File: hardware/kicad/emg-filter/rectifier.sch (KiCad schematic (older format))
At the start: 8 parts, among them U1 LM4565

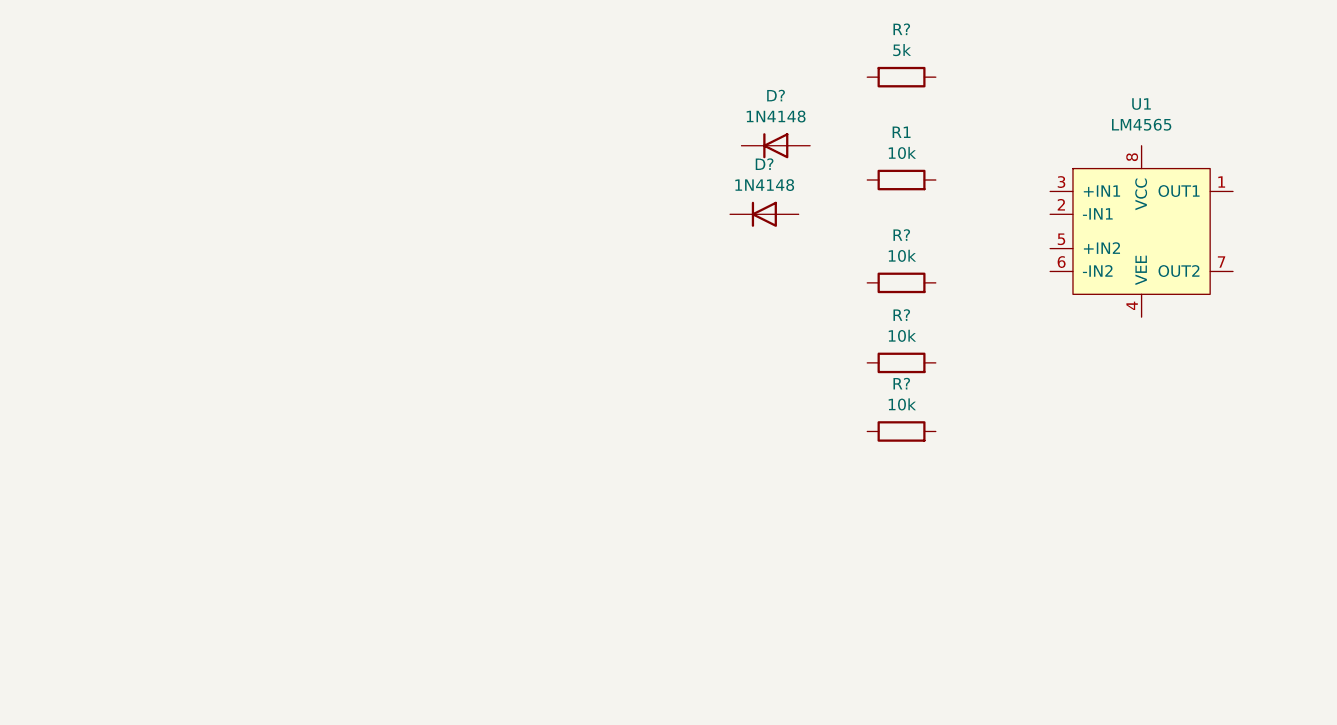
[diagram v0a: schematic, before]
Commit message: Added rectifier diagram
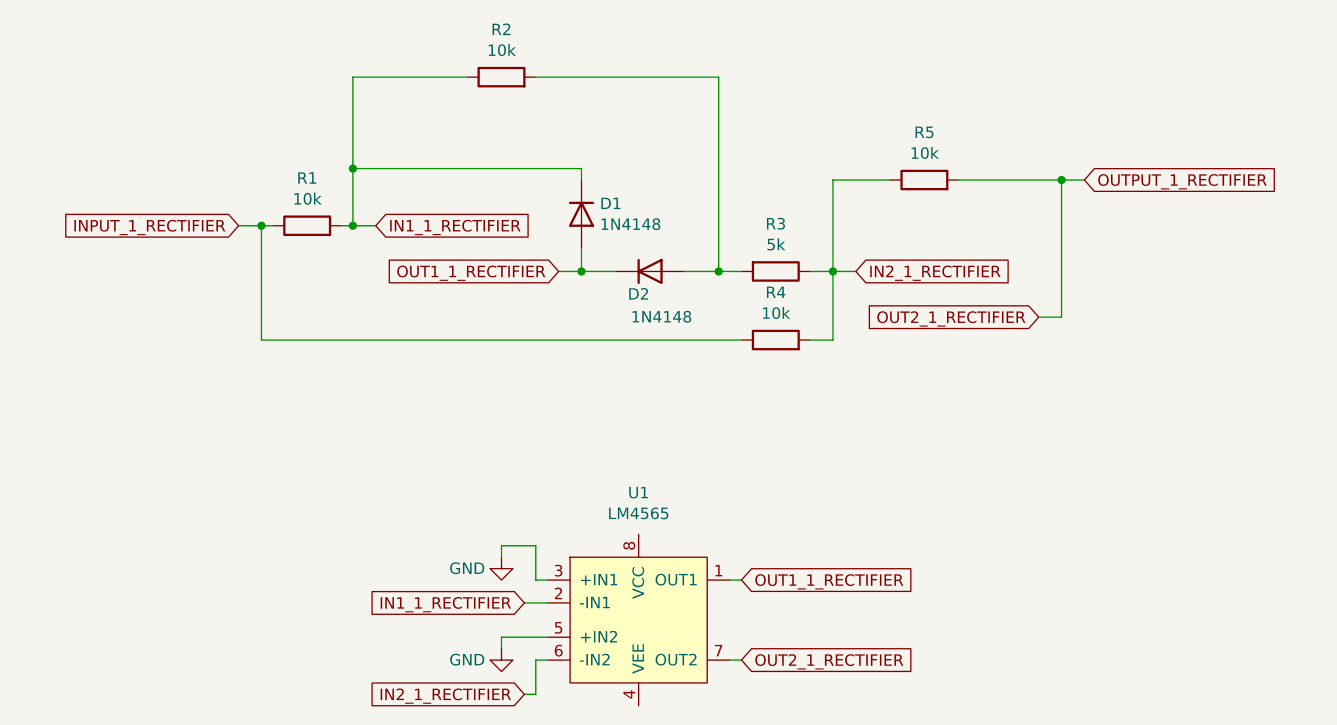
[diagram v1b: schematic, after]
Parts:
- gave numbers to parts that had none: 6
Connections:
- net OUT1_1_RECTIFIER: now reaches U1.1 (OUT1)
- net OUT1_1_RECTIFIER: now also D1.2 (A), D2.1 (K)
- net IN1_1_RECTIFIER: now reaches U1.2 (-IN1)
- net IN1_1_RECTIFIER: now also D1.1 (K), R1.2, R2.1
- net GND: now reaches U1.3 (+IN1)
- net GND: now also U1.5 (+IN2)
- net IN2_1_RECTIFIER: now reaches U1.6 (-IN2)
- net IN2_1_RECTIFIER: now also R3.1, R4.2, R5.1
- net OUT2_1_RECTIFIER: now reaches U1.7 (OUT2)
- net OUT2_1_RECTIFIER: now also R5.2
- net INPUT_1_RECTIFIER: now reaches R1.1
- net INPUT_1_RECTIFIER: now also R4.1
- net at R2.2: now also D2.2 (A), R3.2
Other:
- moved on the sheet: D1, D2, R1, R2, R3, R4, R5, U1
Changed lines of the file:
@@
 L emg-filter:LM4565 U1
 U 1 1 61C39F82
-P 7050 2900
-F 0 "U1" H 7050 3431 50  0000 C CNN
-F 1 "LM4565" H 7050 3340 50  0000 C CNN
-F 2 "" H 8050 2900 50  0001 C CNN
-F 3 "" H 8050 2900 50  0001 C CNN
-	1    7050 2900
+P 4850 4600
+F 0 "U1" H 4850 5131 50  0000 C CNN
+F 1 "LM4565" H 4850 5040 50  0000 C CNN
+F 2 "" H 5850 4600 50  0001 C CNN
+F 3 "" H 5850 4600 50  0001 C CNN
+	1    4850 4600
 	1    0    0    -1
 $EndComp
@@
 L Device:R R1
 U 1 1 61C3AD78
-P 6000 2700
-F 0 "R1" V 6207 2700 50  0000 C CNN
-F 1 "10k" V 6116 2700 50  0000 C CNN
-F 2 "" V 5930 2700 50  0001 C CNN
-F 3 "~" H 6000 2700 50  0001 C CNN
-	1    6000 2700
-	0    -1   -1   0
-$EndComp
-$Comp
-L Device:R R?
+P 3400 2900
+F 0 "R1" V 3607 2900 50  0000 C CNN
+F 1 "10k" V 3516 2900 50  0000 C CNN
+F 2 "" V 3330 2900 50  0001 C CNN
+F 3 "~" H 3400 2900 50  0001 C CNN
+	1    3400 2900
+	0    -1   -1   0
+$EndComp
+$Comp
+L Device:R R2
 U 1 1 61C4805B
-P 6000 3150
-F 0 "R?" V 6207 3150 50  0000 C CNN
-F 1 "10k" V 6116 3150 50  0000 C CNN
-F 2 "" V 5930 3150 50  0001 C CNN
-F 3 "~" H 6000 3150 50  0001 C CNN
-	1    6000 3150
-	0    -1   -1   0
-$EndComp
-$Comp
-L Device:R R?
+P 4250 2250
+F 0 "R2" V 4457 2250 50  0000 C CNN
+F 1 "10k" V 4366 2250 50  0000 C CNN
+F 2 "" V 4180 2250 50  0001 C CNN
+F 3 "~" H 4250 2250 50  0001 C CNN
+	1    4250 2250
+	0    -1   -1   0
+$EndComp
+$Comp
+L Device:R R3
 U 1 1 61C4A9A1
-P 6000 2250
-F 0 "R?" V 5793 2250 50  0000 C CNN
-F 1 "5k" V 5884 2250 50  0000 C CNN
-F 2 "" V 5930 2250 50  0001 C CNN
-F 3 "~" H 6000 2250 50  0001 C CNN
-	1    6000 2250
+P 5450 3100
+F 0 "R3" V 5243 3100 50  0000 C CNN
+F 1 "5k" V 5334 3100 50  0000 C CNN
+F 2 "" V 5380 3100 50  0001 C CNN
+F 3 "~" H 5450 3100 50  0001 C CNN
+	1    5450 3100
 	0    1    1    0
 $EndComp
 $Comp
-L Device:R R?
+L Device:R R5
 U 1 1 61C4B3BB
-P 6000 3500
-F 0 "R?" V 6207 3500 50  0000 C CNN
-F 1 "10k" V 6116 3500 50  0000 C CNN
-F 2 "" V 5930 3500 50  0001 C CNN
-F 3 "~" H 6000 3500 50  0001 C CNN
-	1    6000 3500
-	0    -1   -1   0
-$EndComp
-$Comp
-L Device:R R?
+P 6100 2700
+F 0 "R5" V 6307 2700 50  0000 C CNN
+F 1 "10k" V 6216 2700 50  0000 C CNN
+F 2 "" V 6030 2700 50  0001 C CNN
+F 3 "~" H 6100 2700 50  0001 C CNN
+	1    6100 2700
+	0    -1   -1   0
+$EndComp
+$Comp
+L Device:R R4
 U 1 1 61C4B97C
-P 6000 3800
-F 0 "R?" V 6207 3800 50  0000 C CNN
-F 1 "10k" V 6116 3800 50  0000 C CNN
-F 2 "" V 5930 3800 50  0001 C CNN
-F 3 "~" H 6000 3800 50  0001 C CNN
-	1    6000 3800
-	0    -1   -1   0
-$EndComp
-$Comp
-L Device:D D?
+P 5450 3400
+F 0 "R4" V 5657 3400 50  0000 C CNN
+F 1 "10k" V 5566 3400 50  0000 C CNN
+F 2 "" V 5380 3400 50  0001 C CNN
+F 3 "~" H 5450 3400 50  0001 C CNN
+	1    5450 3400
+	0    -1   -1   0
+$EndComp
+$Comp
+L Device:D D2
 U 1 1 61C4C7DA
-P 5450 2550
-F 0 "D?" H 5450 2767 50  0000 C CNN
-F 1 "1N4148" H 5450 2676 50  0000 C CNN
-F 2 "" H 5450 2550 50  0001 C CNN
-F 3 "~" H 5450 2550 50  0001 C CNN
-	1    5450 2550
-	1    0    0    -1
-$EndComp
-$Comp
-L Device:D D?
+P 4900 3100
+F 0 "D2" H 4850 3000 50  0000 C CNN
+F 1 "1N4148" H 4950 2900 50  0000 C CNN
+F 2 "" H 4900 3100 50  0001 C CNN
+F 3 "~" H 4900 3100 50  0001 C CNN
+	1    4900 3100
+	1    0    0    -1
+$EndComp
+$Comp
+L Device:D D1
 U 1 1 61C4C9DB
-P 5400 2850
-F 0 "D?" H 5400 3067 50  0000 C CNN
-F 1 "1N4148" H 5400 2976 50  0000 C CNN
-F 2 "" H 5400 2850 50  0001 C CNN
-F 3 "~" H 5400 2850 50  0001 C CNN
-	1    5400 2850
-	1    0    0    -1
-$EndComp
+P 4600 2850
+F 0 "D1" V 4554 2930 50  0000 L CNN
+F 1 "1N4148" V 4645 2930 50  0000 L CNN
+F 2 "" H 4600 2850 50  0001 C CNN
+F 3 "~" H 4600 2850 50  0001 C CNN
+	1    4600 2850
+	0    1    1    0
+$EndComp
+Wire Wire Line
+	3600 2250 4100 2250
+Wire Wire Line
+	4600 2700 4600 2650
+Wire Wire Line
+	4600 2650 3600 2650
+Wire Wire Line
+	3600 2650 3600 2250
+Wire Wire Line
+	3600 2650 3600 2900
+Wire Wire Line
+	3600 2900 3550 2900
+Connection ~ 3600 2650
+Text GLabel 5300 4450 2    50   Input ~ 0
+OUT1_1_RECTIFIER
+Text GLabel 4500 3100 0    50   Input ~ 0
+OUT1_1_RECTIFIER
+Wire Wire Line
+	4600 3000 4600 3100
+Wire Wire Line
+	5200 3100 5200 2250
+Wire Wire Line
+	5200 2250 4400 2250
+Wire Wire Line
+	5200 3100 5300 3100
+Wire Wire Line
+	4600 3100 4750 3100
+Wire Wire Line
+	5050 3100 5200 3100
+Connection ~ 5200 3100
+Text GLabel 3700 2900 2    50   Input ~ 0
+IN1_1_RECTIFIER
+Wire Wire Line
+	4500 3100 4600 3100
+Connection ~ 4600 3100
+Wire Wire Line
+	3600 2900 3700 2900
+Connection ~ 3600 2900
+Text GLabel 4350 4550 0    50   Input ~ 0
+IN1_1_RECTIFIER
+Wire Wire Line
+	5250 4450 5300 4450
+$Comp
+L power:GND #PWR01
+U 1 1 61C650AA
+P 4250 4350
+F 0 "#PWR01" H 4250 4100 50  0001 C CNN
+F 1 "GND" H 4100 4300 50  0000 C CNN
+F 2 "" H 4250 4350 50  0001 C CNN
+F 3 "" H 4250 4350 50  0001 C CNN
+	1    4250 4350
+	1    0    0    -1
+$EndComp
+Wire Wire Line
+	3250 2900 3200 2900
+Wire Wire Line
+	3200 3400 5300 3400
+Wire Wire Line
+	3200 2900 3200 3400
+Wire Wire Line
+	5600 3400 5700 3400
+Wire Wire Line
+	5700 3400 5700 3100
+Wire Wire Line
+	5700 3100 5600 3100
+Wire Wire Line
+	5700 3100 5700 2700
+Wire Wire Line
+	5700 2700 5950 2700
+Connection ~ 5700 3100
+Text GLabel 5800 3100 2    50   Input ~ 0
+IN2_1_RECTIFIER
+Wire Wire Line
+	5700 3100 5800 3100
+Text GLabel 4350 4950 0    50   Input ~ 0
+IN2_1_RECTIFIER
+$Comp
+L power:GND #PWR02
+U 1 1 61C6C0BF
+P 4250 4750
+F 0 "#PWR02" H 4250 4500 50  0001 C CNN
+F 1 "GND" H 4100 4700 50  0000 C CNN
+F 2 "" H 4250 4750 50  0001 C CNN
+F 3 "" H 4250 4750 50  0001 C CNN
+	1    4250 4750
+	1    0    0    -1
+$EndComp
+Wire Wire Line
+	4450 4700 4250 4700
+Wire Wire Line
+	4450 4550 4350 4550
+Text GLabel 5300 4800 2    50   Input ~ 0
+OUT2_1_RECTIFIER
+Wire Wire Line
+	5250 4800 5300 4800
+Text GLabel 6600 3300 0    50   Input ~ 0
+OUT2_1_RECTIFIER
+Wire Wire Line
+	6600 3300 6700 3300
+Wire Wire Line
+	6700 3300 6700 2700
+Wire Wire Line
+	6700 2700 6250 2700
+Wire Wire Line
+	4450 4800 4400 4800
+Wire Wire Line
+	4400 4800 4400 4950
+Wire Wire Line
+	4400 4950 4350 4950
+Wire Wire Line
+	4450 4450 4400 4450
+Wire Wire Line
+	4400 4450 4400 4300
+Wire Wire Line
+	4400 4300 4250 4300
+Text GLabel 3100 2900 0    50   Input ~ 0
+INPUT_1_RECTIFIER
+Wire Wire Line
+	3200 2900 3100 2900
+Connection ~ 3200 2900
+Text GLabel 6800 2700 2    50   Input ~ 0
+OUTPUT_1_RECTIFIER
+Wire Wire Line
+	6800 2700 6700 2700
+Connection ~ 6700 2700
+Wire Wire Line
+	4250 4700 4250 4750
+Wire Wire Line
+	4250 4300 4250 4350
 $EndSCHEMATC

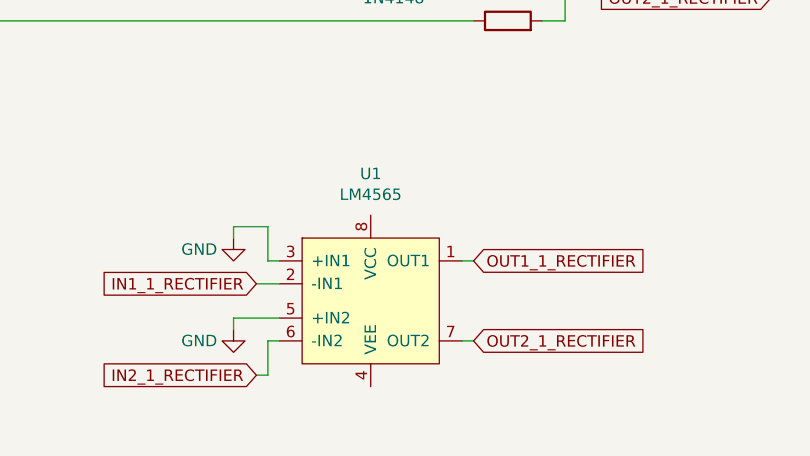
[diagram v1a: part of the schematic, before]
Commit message: Rectifier implemented
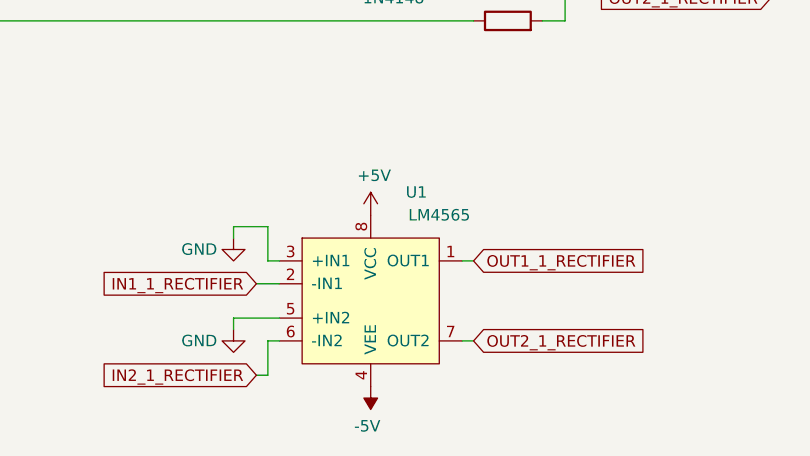
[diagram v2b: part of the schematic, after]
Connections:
- net -5V: now reaches U1.4 (VEE)
- net +5V: now reaches U1.8 (VCC)
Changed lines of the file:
@@
 U 1 1 61C39F82
 P 4850 4600
-F 0 "U1" H 4850 5131 50  0000 C CNN
-F 1 "LM4565" H 4850 5040 50  0000 C CNN
+F 0 "U1" H 5050 5050 50  0000 C CNN
+F 1 "LM4565" H 5150 4950 50  0000 C CNN
 F 2 "" H 5850 4600 50  0001 C CNN
 F 3 "" H 5850 4600 50  0001 C CNN
@@
 Wire Wire Line
 	4250 4300 4250 4350
+$Comp
+L power:+5V #PWR?
+U 1 1 61C415B3
+P 4850 4250
+F 0 "#PWR?" H 4850 4100 50  0001 C CNN
+F 1 "+5V" H 4865 4423 50  0000 C CNN
+F 2 "" H 4850 4250 50  0001 C CNN
+F 3 "" H 4850 4250 50  0001 C CNN
+	1    4850 4250
+	1    0    0    -1
+$EndComp
+$Comp
+L power:-5V #PWR?
+U 1 1 61C41B44
+P 4850 5000
+F 0 "#PWR?" H 4850 5100 50  0001 C CNN
+F 1 "-5V" H 4865 5173 50  0000 C CNN
+F 2 "" H 4850 5000 50  0001 C CNN
+F 3 "" H 4850 5000 50  0001 C CNN
+	1    4850 5000
+	-1   0    0    1
+$EndComp
 $EndSCHEMATC

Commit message: 16 rectifiers.
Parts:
- added D10, D11, D12, D13, D14, D15, D16, D17, D18, D19, D20, D21, D22, D23, D24, D25, D26, D27, D28, D29, D3, D30, D31, D32, D4, D5, D6, D7, D8, D9: 1N4148, symbol Device:D
- added R10, R11, R12, R13, R14, R15, R16, R17, R18, R19, R21, R23, R25, R27, R29, R31, R33, R34, R35, R36, R37, R38, R39, R40, R41, R42, R43, R44, R45, R46, R47, R48, R49, R50, R51, R52, R53, R54, R55, R56, R58, R6, R60, R62, R64, R66, R68, R7, R70, R72, R73, R74, R75, R76, R77, R78, R79, R8, R80, R9: 10k, symbol Device:R
- added R20, R22, R24, R26, R28, R30, R32, R57, R59, R61, R63, R65, R67, R69, R71: 5k, symbol Device:R
- added U10, U11, U12, U13, U14, U15, U16, U2, U3, U4, U5, U6, U7, U8, U9: LM4565, symbol emg-filter:LM4565
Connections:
- net +5V: now also U10.8 (VCC), U11.8 (VCC), U12.8 (VCC), U13.8 (VCC), U14.8 (VCC), U15.8 (VCC), U16.8 (VCC), U2.8 (VCC), U3.8 (VCC), U4.8 (VCC), U5.8 (VCC), U6.8 (VCC), U7.8 (VCC), U8.8 (VCC), U9.8 (VCC)
- net -5V: now also U10.4 (VEE), U11.4 (VEE), U12.4 (VEE), U13.4 (VEE), U14.4 (VEE), U15.4 (VEE), U16.4 (VEE), U2.4 (VEE), U3.4 (VEE), U4.4 (VEE), U5.4 (VEE), U6.4 (VEE), U7.4 (VEE), U8.4 (VEE), U9.4 (VEE)
- net GND: now also U10.3 (+IN1), U10.5 (+IN2), U11.3 (+IN1), U11.5 (+IN2), U12.3 (+IN1), U12.5 (+IN2), U13.3 (+IN1), U13.5 (+IN2), U14.3 (+IN1), U14.5 (+IN2), U15.3 (+IN1), U15.5 (+IN2), U16.3 (+IN1), U16.5 (+IN2), U2.3 (+IN1), U2.5 (+IN2), U3.3 (+IN1), U3.5 (+IN2), U4.3 (+IN1), U4.5 (+IN2), U5.3 (+IN1), U5.5 (+IN2), U6.3 (+IN1), U6.5 (+IN2), U7.3 (+IN1), U7.5 (+IN2), U8.3 (+IN1), U8.5 (+IN2), U9.3 (+IN1), U9.5 (+IN2)
- new net: D10.2 (A), R13.2, R20.2
- new net: D11.2 (A), R14.2, R22.2
- new net: D12.2 (A), R15.2, R24.2
- new net: D13.2 (A), R16.2, R26.2
- new net: D14.2 (A), R17.2, R28.2
- new net: D15.2 (A), R18.2, R30.2
- new net: D16.2 (A), R19.2, R32.2
- new net: D29.2 (A), R53.2, R65.2
- new net: D26.2 (A), R50.2, R59.2
- new net: D27.2 (A), R51.2, R61.2
- new net: D28.2 (A), R52.2, R63.2
- new net: D25.2 (A), R49.2, R57.2
- new net: D31.2 (A), R55.2, R69.2
- new net: D32.2 (A), R56.2, R71.2
- new net: D30.2 (A), R54.2, R67.2
- new net IN1_10_RECTIFIER: D18.1 (K), R42.2, R50.1, U10.2 (-IN1)
- new net IN1_11_RECTIFIER: D19.1 (K), R43.2, R51.1, U11.2 (-IN1)
- new net IN1_12_RECTIFIER: D20.1 (K), R44.2, R52.1, U12.2 (-IN1)
- new net IN1_13_RECTIFIER: D17.1 (K), R41.2, R49.1, U9.2 (-IN1)
- new net IN1_14_RECTIFIER: D23.1 (K), R47.2, R55.1, U15.2 (-IN1)
- new net IN1_15_RECTIFIER: D24.1 (K), R48.2, R56.1, U16.2 (-IN1)
- new net IN1_16_RECTIFIER: D22.1 (K), R46.2, R54.1, U14.2 (-IN1)
- new net IN1_2_RECTIFIER: D3.1 (K), R13.1, R6.2, U2.2 (-IN1)
- new net IN1_3_RECTIFIER: D4.1 (K), R14.1, R7.2, U3.2 (-IN1)
- new net IN1_4_RECTIFIER: D5.1 (K), R15.1, R8.2, U4.2 (-IN1)
- new net IN1_5_RECTIFIER: D6.1 (K), R16.1, R9.2, U5.2 (-IN1)
- new net IN1_6_RECTIFIER: D7.1 (K), R10.2, R17.1, U6.2 (-IN1)
- new net IN1_7_RECTIFIER: D8.1 (K), R11.2, R18.1, U7.2 (-IN1)
- new net IN1_8_RECTIFIER: D9.1 (K), R12.2, R19.1, U8.2 (-IN1)
- new net IN1_9_RECTIFIER: D21.1 (K), R45.2, R53.1, U13.2 (-IN1)
- new net IN2_10_RECTIFIER: R59.1, R60.2, R74.1, U10.6 (-IN2)
- new net IN2_11_RECTIFIER: R61.1, R62.2, R75.1, U11.6 (-IN2)
- new net IN2_12_RECTIFIER: R63.1, R64.2, R76.1, U12.6 (-IN2)
- new net IN2_13_RECTIFIER: R57.1, R58.2, R73.1, U9.6 (-IN2)
- new net IN2_14_RECTIFIER: R69.1, R70.2, R79.1, U15.6 (-IN2)
- new net IN2_15_RECTIFIER: R71.1, R72.2, R80.1, U16.6 (-IN2)
- new net IN2_16_RECTIFIER: R67.1, R68.2, R78.1, U14.6 (-IN2)
- new net IN2_2_RECTIFIER: R20.1, R21.2, R34.1, U2.6 (-IN2)
- new net IN2_3_RECTIFIER: R22.1, R23.2, R35.1, U3.6 (-IN2)
- new net IN2_4_RECTIFIER: R24.1, R25.2, R36.1, U4.6 (-IN2)
- new net IN2_5_RECTIFIER: R26.1, R27.2, R37.1, U5.6 (-IN2)
- new net IN2_6_RECTIFIER: R28.1, R29.2, R38.1, U6.6 (-IN2)
- new net IN2_7_RECTIFIER: R30.1, R31.2, R39.1, U7.6 (-IN2)
- new net IN2_8_RECTIFIER: R32.1, R33.2, R40.1, U8.6 (-IN2)
- new net IN2_9_RECTIFIER: R65.1, R66.2, R77.1, U13.6 (-IN2)
- new net INPUT_10_RECTIFIER: R42.1, R60.1
- new net INPUT_11_RECTIFIER: R43.1, R62.1
- new net INPUT_12_RECTIFIER: R44.1, R64.1
- new net INPUT_13_RECTIFIER: R41.1, R58.1
- new net INPUT_14_RECTIFIER: R47.1, R70.1
- new net INPUT_15_RECTIFIER: R48.1, R72.1
- new net INPUT_16_RECTIFIER: R46.1, R68.1
- new net INPUT_2_RECTIFIER: R21.1, R6.1
- new net INPUT_3_RECTIFIER: R23.1, R7.1
- new net INPUT_4_RECTIFIER: R25.1, R8.1
- new net INPUT_5_RECTIFIER: R27.1, R9.1
- new net INPUT_6_RECTIFIER: R10.1, R29.1
- new net INPUT_7_RECTIFIER: R11.1, R31.1
- new net INPUT_8_RECTIFIER: R12.1, R33.1
- new net INPUT_9_RECTIFIER: R45.1, R66.1
- new net OUT1_10_RECTIFIER: D18.2 (A), D26.1 (K), U10.1 (OUT1)
- new net OUT1_11_RECTIFIER: D19.2 (A), D27.1 (K), U11.1 (OUT1)
- new net OUT1_12_RECTIFIER: D20.2 (A), D28.1 (K), U12.1 (OUT1)
- new net OUT1_13_RECTIFIER: D17.2 (A), D25.1 (K), U9.1 (OUT1)
- new net OUT1_14_RECTIFIER: D23.2 (A), D31.1 (K), U15.1 (OUT1)
- new net OUT1_15_RECTIFIER: D24.2 (A), D32.1 (K), U16.1 (OUT1)
- new net OUT1_16_RECTIFIER: D22.2 (A), D30.1 (K), U14.1 (OUT1)
- new net OUT1_2_RECTIFIER: D10.1 (K), D3.2 (A), U2.1 (OUT1)
- new net OUT1_3_RECTIFIER: D11.1 (K), D4.2 (A), U3.1 (OUT1)
- new net OUT1_4_RECTIFIER: D12.1 (K), D5.2 (A), U4.1 (OUT1)
- new net OUT1_5_RECTIFIER: D13.1 (K), D6.2 (A), U5.1 (OUT1)
- new net OUT1_6_RECTIFIER: D14.1 (K), D7.2 (A), U6.1 (OUT1)
- new net OUT1_7_RECTIFIER: D15.1 (K), D8.2 (A), U7.1 (OUT1)
- new net OUT1_8_RECTIFIER: D16.1 (K), D9.2 (A), U8.1 (OUT1)
- new net OUT1_9_RECTIFIER: D21.2 (A), D29.1 (K), U13.1 (OUT1)
- new net OUT2_10_RECTIFIER: R74.2, U10.7 (OUT2)
- new net OUT2_11_RECTIFIER: R75.2, U11.7 (OUT2)
- new net OUT2_12_RECTIFIER: R76.2, U12.7 (OUT2)
- new net OUT2_13_RECTIFIER: R73.2, U9.7 (OUT2)
- new net OUT2_14_RECTIFIER: R79.2, U15.7 (OUT2)
- new net OUT2_15_RECTIFIER: R80.2, U16.7 (OUT2)
- new net OUT2_16_RECTIFIER: R78.2, U14.7 (OUT2)
- new net OUT2_2_RECTIFIER: R34.2, U2.7 (OUT2)
- new net OUT2_3_RECTIFIER: R35.2, U3.7 (OUT2)
- new net OUT2_4_RECTIFIER: R36.2, U4.7 (OUT2)
- new net OUT2_5_RECTIFIER: R37.2, U5.7 (OUT2)
- new net OUT2_6_RECTIFIER: R38.2, U6.7 (OUT2)
- new net OUT2_7_RECTIFIER: R39.2, U7.7 (OUT2)
- new net OUT2_8_RECTIFIER: R40.2, U8.7 (OUT2)
- new net OUT2_9_RECTIFIER: R77.2, U13.7 (OUT2)
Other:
- moved on the sheet: D1, D2, R1, R2, R3, R4, R5, U1
